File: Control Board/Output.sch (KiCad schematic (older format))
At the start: 24 parts, among them Q1 MMBT2222, Q2 MMBT2222, Q3 AOD403

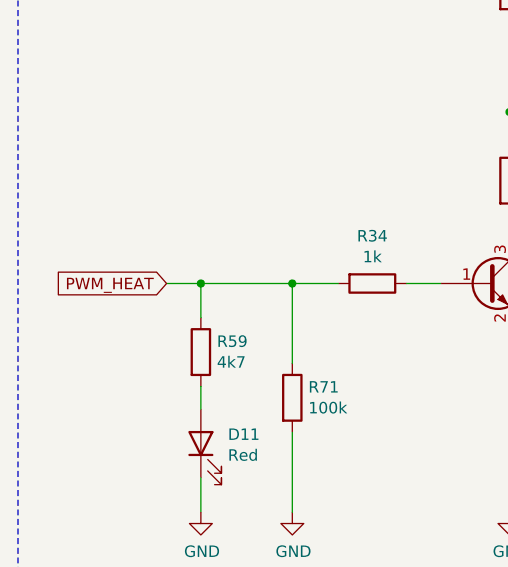
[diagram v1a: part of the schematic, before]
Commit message: Samd21 D2, D4 where swapped in symbol. No pcb change.
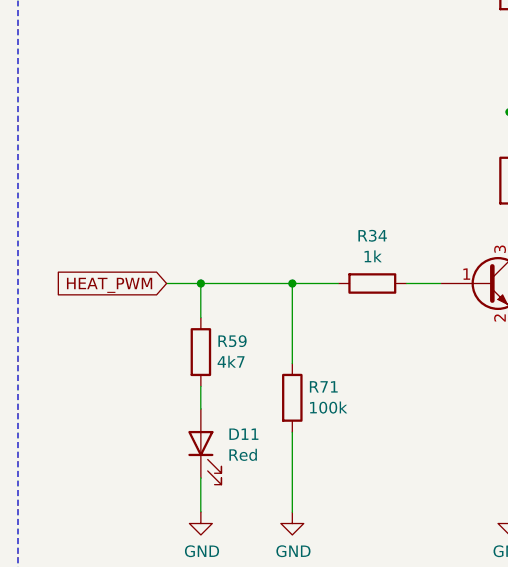
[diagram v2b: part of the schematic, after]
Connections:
- net PWM_HEAT renamed HEAT_PWM
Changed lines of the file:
@@
 Sheet 5 5
 Title "IoT12-hardware output"
-Date "2021-03-08"
-Rev "V2.0"
+Date "2021-03-12"
+Rev "V2.1"
 Comp ""
 Comment1 ""
@@
 	2250 2750 2400 2750
 Text GLabel 1200 2750 0    50   Input ~ 0
-PWM_HEAT
+HEAT_PWM
 Wire Wire Line
 	1200 2750 1350 2750

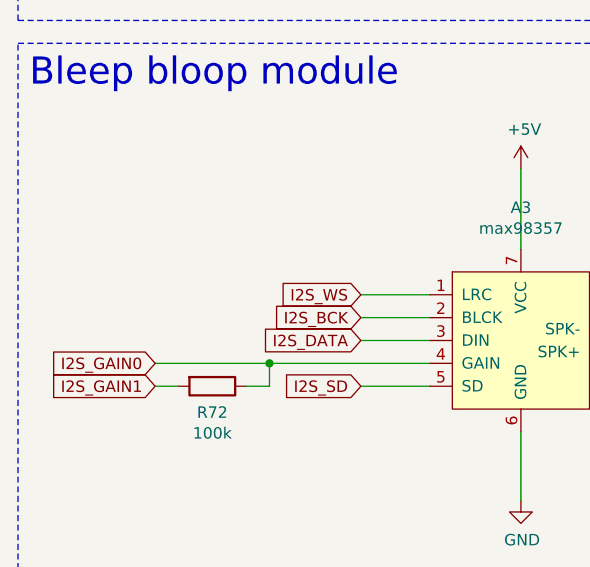
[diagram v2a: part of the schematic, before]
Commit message: Not all GAIN combinations are possible.
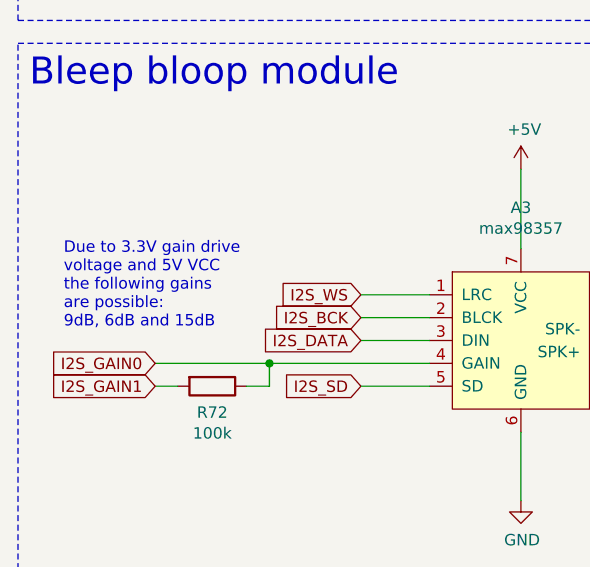
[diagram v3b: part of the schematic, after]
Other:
- note added: "Due to 3.3V gain drive\nvoltage and 5V VCC \nthe following gains \nare possible:\n9dB, 6dB and 15dB"
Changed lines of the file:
@@
 Text Label 2750 2000 0    50   ~ 0
 GATE
+Text Notes 750  5450 0    50   ~ 0
+Due to 3.3V gain drive\nvoltage and 5V VCC \nthe following gains \nare possible:\n9dB, 6dB and 15dB
 $EndSCHEMATC

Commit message: Corrected errors.
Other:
- note added: "Due to 3.3V gain drive\nvoltage and 5V VCC \nthe following gains \nare possible:\n9dB, 12dB and 15dB"
- note removed: "Due to 3.3V gain drive\nvoltage and 5V VCC \nthe following gains \nare possible:\n9dB, 6dB and 15dB"
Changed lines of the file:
@@
 GATE
 Text Notes 750  5450 0    50   ~ 0
-Due to 3.3V gain drive\nvoltage and 5V VCC \nthe following gains \nare possible:\n9dB, 6dB and 15dB
+Due to 3.3V gain drive\nvoltage and 5V VCC \nthe following gains \nare possible:\n9dB, 12dB and 15dB
 $EndSCHEMATC
